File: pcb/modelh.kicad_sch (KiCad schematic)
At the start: 45 parts, among them SW1 SW_Push, U1 GD32F103C8T6, U2 AMS1117-3.3, Y1 8MHz

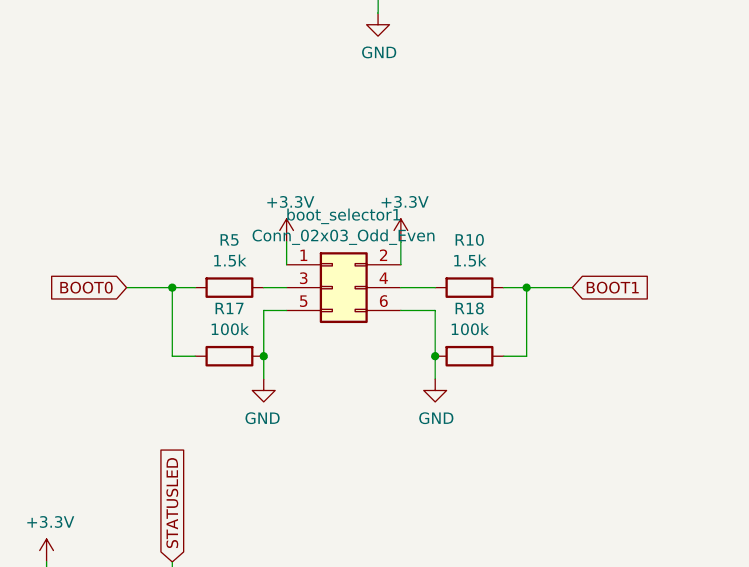
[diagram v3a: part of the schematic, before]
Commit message: Updates silkscreen to make clear boot selector
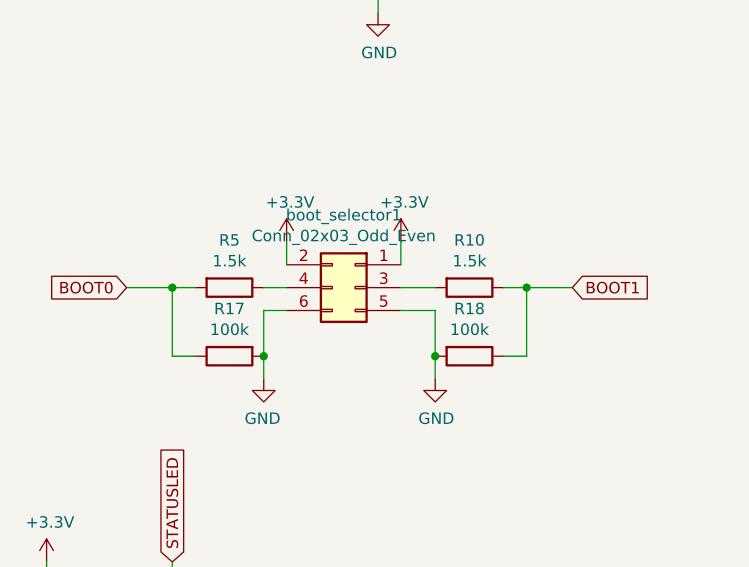
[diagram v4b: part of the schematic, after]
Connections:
- net at R10.2: now also boot_selector1.3 (Pin_3); no longer boot_selector1.4 (Pin_4)
- net at R5.1: now also boot_selector1.4 (Pin_4); no longer boot_selector1.3 (Pin_3)

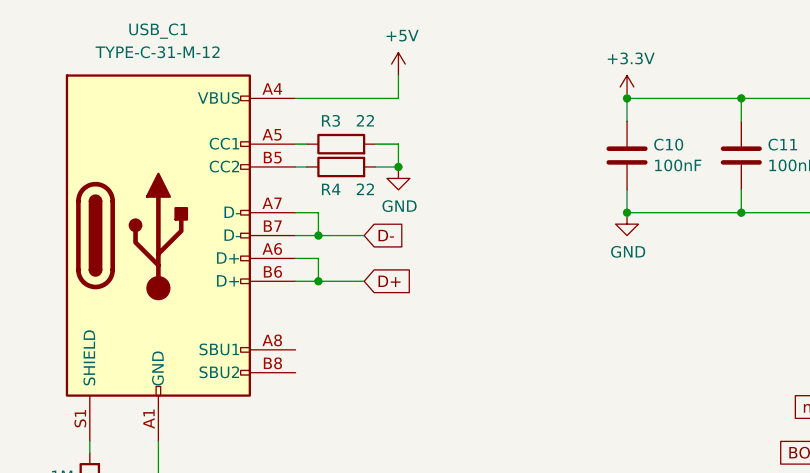
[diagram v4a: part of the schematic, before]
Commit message: Adds missing 1.5k pullup resistor to USB D+ line
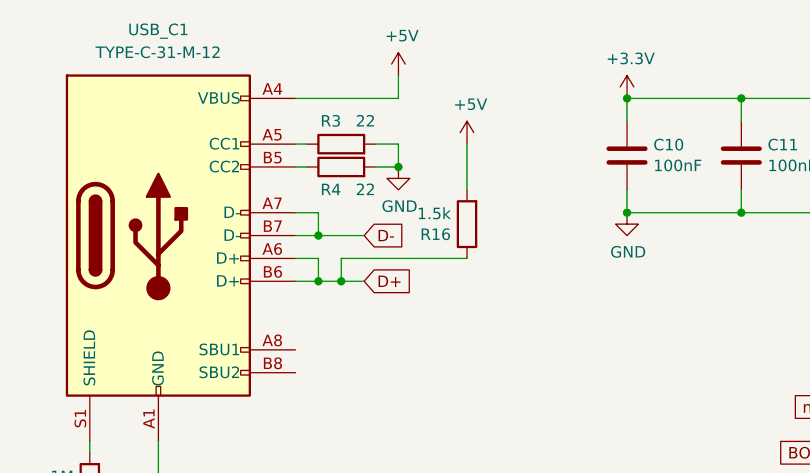
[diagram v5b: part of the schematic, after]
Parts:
- added R16: 1.5k, Resistor_SMD:R_0603_1608Metric, symbol Device:R
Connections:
- net +5V: now also R16.2
- net D+: now also R16.1
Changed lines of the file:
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@@
   (junction (at 121.92 39.37) (diameter 0) (color 0 0 0 0)
+  )
+  (junction (at 64.77 46.99) (diameter 0) (color 0 0 0 0)
   )
   (junction (at 180.34 43.18) (diameter 0) (color 0 0 0 0)
@@
     (stroke (width 0) (type default) (color 0 0 0 0))
   )
+  (wire (pts (xy 64.77 46.99) (xy 67.31 46.99))
+    (stroke (width 0) (type default) (color 0 0 0 0))
+  )
   (wire (pts (xy 67.31 88.9) (xy 72.39 88.9))
     (stroke (width 0) (type default) (color 0 0 0 0))
@@
     (stroke (width 0) (type default) (color 0 0 0 0))
   )
+  (wire (pts (xy 64.77 44.45) (xy 64.77 46.99))
+    (stroke (width 0) (type default) (color 0 0 0 0))
+  )
   (wire (pts (xy 72.39 88.9) (xy 83.82 88.9))
     (stroke (width 0) (type default) (color 0 0 0 0))
@@
     (stroke (width 0) (type default) (color 0 0 0 0))
   )
+  (wire (pts (xy 78.74 31.75) (xy 78.74 36.83))
+    (stroke (width 0) (type default) (color 0 0 0 0))
+  )
   (wire (pts (xy 248.92 49.53) (xy 255.27 49.53))
     (stroke (width 0) (type default) (color 0 0 0 0))
@@
     (stroke (width 0) (type default) (color 0 0 0 0))
   )
-  (wire (pts (xy 62.23 46.99) (xy 67.31 46.99))
+  (wire (pts (xy 62.23 46.99) (xy 64.77 46.99))
+    (stroke (width 0) (type default) (color 0 0 0 0))
+  )
+  (wire (pts (xy 78.74 44.45) (xy 64.77 44.45))
     (stroke (width 0) (type default) (color 0 0 0 0))
   )
@@
     (pin "4")
   )
+  (symbol (lib_id "power:+5V") (at 78.74 31.75 0) (unit 1)
+    (in_bom yes) (on_board yes)
+    (property "Reference" "#PWR0127" (id 0) (at 78.74 35.56 0)
+      (effects (font (size 1.27 1.27)) hide)
+    )
+    (property "Value" "+5V" (id 1) (at 79.121 27.3558 0))
+    (property "Footprint" "" (id 2) (at 78.74 31.75 0)
+      (effects (font (size 1.27 1.27)) hide)
+    )
+    (property "Datasheet" "" (id 3) (at 78.74 31.75 0)
+      (effects (font (size 1.27 1.27)) hide)
+    )
+    (pin "1")
+  )
   (symbol (lib_id "Connector:USB_C_Receptacle_USB2.0") (at 44.45 41.91 0) (unit 1)
     (in_bom yes) (on_board yes) (fields_autoplaced)
@@
     (pin "S1")
   )
+  (symbol (lib_id "Device:R") (at 78.74 40.64 180) (unit 1)
+    (in_bom yes) (on_board yes)
+    (property "Reference" "R16" (id 0) (at 76.962 41.8084 0)
+      (effects (font (size 1.27 1.27)) (justify left))
+    )
+    (property "Value" "1.5k" (id 1) (at 76.962 39.497 0)
+      (effects (font (size 1.27 1.27)) (justify left))
+    )
+    (property "Footprint" "Resistor_SMD:R_0603_1608Metric" (id 2) (at 80.518 40.64 90)
+      (effects (font (size 1.27 1.27)) hide)
+    )
+    (property "Datasheet" "~" (id 3) (at 78.74 40.64 0)
+      (effects (font (size 1.27 1.27)) hide)
+    )
+    (property "LCSC" "C22843" (id 4) (at 78.74 40.64 0)
+      (effects (font (size 1.27 1.27)) hide)
+    )
+    (pin "1")
+    (pin "2")
+  )
   (symbol (lib_id "TE-6-520315-6:6-520315-6") (at 255.27 69.85 0) (mirror x) (unit 1)
     (in_bom yes) (on_board yes)
@@
       (reference "#PWR0126") (unit 1) (value "+5V") (footprint "")
     )
+    (path "/449da5ab-c6ac-45b5-bcdc-f492eee962dc"
+      (reference "#PWR0127") (unit 1) (value "+5V") (footprint "")
+    )
     (path "/00000000-0000-0000-0000-00005f28cee3"
       (reference "C1") (unit 1) (value "10uF") (footprint "Capacitor_SMD:C_0603_1608Metric")
@@
       (reference "R15") (unit 1) (value "0") (footprint "Resistor_SMD:R_0805_2012Metric_Pad1.15x1.40mm_HandSolder")
     )
+    (path "/79b2448b-a329-4291-a39b-4d2e35c6ecb6"
+      (reference "R16") (unit 1) (value "1.5k") (footprint "Resistor_SMD:R_0603_1608Metric")
+    )
     (path "/00000000-0000-0000-0000-00005f1d1ef2"

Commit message: Update schematics and pcb
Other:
- moved on the sheet: TP1, custom_leds_A1
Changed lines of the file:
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@@
   (no_connect (at 129.54 83.82))
   (no_connect (at 129.54 81.28))
-  (wire (pts (xy 227.33 151.13) (xy 240.03 151.13))
+  (wire (pts (xy 207.01 151.13) (xy 219.71 151.13))
     (stroke (width 0) (type default) (color 0 0 0 0))
   )
@@
     (stroke (width 0) (type default) (color 0 0 0 0))
   )
-  (wire (pts (xy 227.33 153.67) (xy 240.03 153.67))
+  (wire (pts (xy 207.01 153.67) (xy 219.71 153.67))
     (stroke (width 0) (type default) (color 0 0 0 0))
   )
@@
     (stroke (width 0) (type default) (color 0 0 0 0))
   )
-  (wire (pts (xy 240.03 146.05) (xy 237.49 146.05))
+  (wire (pts (xy 219.71 146.05) (xy 217.17 146.05))
     (stroke (width 0) (type default) (color 0 0 0 0))
   )
@@
     (stroke (width 0) (type default) (color 0 0 0 0))
   )
-  (wire (pts (xy 227.33 151.13) (xy 227.33 149.86))
+  (wire (pts (xy 207.01 151.13) (xy 207.01 149.86))
     (stroke (width 0) (type default) (color 0 0 0 0))
   )
@@
     (stroke (width 0) (type default) (color 0 0 0 0))
   )
-  (wire (pts (xy 240.03 143.51) (xy 237.49 143.51))
+  (wire (pts (xy 219.71 143.51) (xy 217.17 143.51))
     (stroke (width 0) (type default) (color 0 0 0 0))
   )
@@
     (stroke (width 0) (type default) (color 0 0 0 0))
   )
-  (wire (pts (xy 237.49 148.59) (xy 240.03 148.59))
+  (wire (pts (xy 217.17 148.59) (xy 219.71 148.59))
     (stroke (width 0) (type default) (color 0 0 0 0))
   )
@@
     (stroke (width 0) (type default) (color 0 0 0 0))
   )
-  (wire (pts (xy 227.33 153.67) (xy 227.33 156.21))
+  (wire (pts (xy 207.01 153.67) (xy 207.01 156.21))
     (stroke (width 0) (type default) (color 0 0 0 0))
   )
@@
     )
   )
-  (global_label "led2" (shape input) (at 237.49 148.59 180) (fields_autoplaced)
-    (effects (font (size 1.27 1.27)) (justify right))
-    (property "Intersheet References" "${INTERSHEET_REFS}" (id 0) (at 0 0 0)
+  (global_label "led2" (shape input) (at 217.17 148.59 180) (fields_autoplaced)
+    (effects (font (size 1.27 1.27)) (justify right))
+    (property "Intersheet References" "${INTERSHEET_REFS}" (id 0) (at -20.32 0 0)
       (effects (font (size 1.27 1.27)) hide)
     )
@@
     )
   )
-  (global_label "led1" (shape input) (at 237.49 146.05 180) (fields_autoplaced)
-    (effects (font (size 1.27 1.27)) (justify right))
-    (property "Intersheet References" "${INTERSHEET_REFS}" (id 0) (at 0 0 0)
+  (global_label "led1" (shape input) (at 217.17 146.05 180) (fields_autoplaced)
+    (effects (font (size 1.27 1.27)) (justify right))
+    (property "Intersheet References" "${INTERSHEET_REFS}" (id 0) (at -20.32 0 0)
       (effects (font (size 1.27 1.27)) hide)
     )
@@
     )
   )
-  (global_label "led0" (shape input) (at 237.49 143.51 180) (fields_autoplaced)
-    (effects (font (size 1.27 1.27)) (justify right))
-    (property "Intersheet References" "${INTERSHEET_REFS}" (id 0) (at 0 0 0)
+  (global_label "led0" (shape input) (at 217.17 143.51 180) (fields_autoplaced)
+    (effects (font (size 1.27 1.27)) (justify right))
+    (property "Intersheet References" "${INTERSHEET_REFS}" (id 0) (at -20.32 0 0)
       (effects (font (size 1.27 1.27)) hide)
     )
@@
     (pin "2")
   )
-  (symbol (lib_id "power:+3.3V") (at 227.33 149.86 0) (unit 1)
-    (in_bom yes) (on_board yes)
-    (property "Reference" "#PWR0119" (id 0) (at 227.33 153.67 0)
-      (effects (font (size 1.27 1.27)) hide)
-    )
-    (property "Value" "+3.3V" (id 1) (at 227.711 145.4658 0))
-    (property "Footprint" "" (id 2) (at 227.33 149.86 0)
-      (effects (font (size 1.27 1.27)) hide)
-    )
-    (property "Datasheet" "" (id 3) (at 227.33 149.86 0)
+  (symbol (lib_id "power:+3.3V") (at 207.01 149.86 0) (unit 1)
+    (in_bom yes) (on_board yes)
+    (property "Reference" "#PWR0119" (id 0) (at 207.01 153.67 0)
+      (effects (font (size 1.27 1.27)) hide)
+    )
+    (property "Value" "+3.3V" (id 1) (at 207.391 145.4658 0))
+    (property "Footprint" "" (id 2) (at 207.01 149.86 0)
+      (effects (font (size 1.27 1.27)) hide)
+    )
+    (property "Datasheet" "" (id 3) (at 207.01 149.86 0)
       (effects (font (size 1.27 1.27)) hide)
     )
@@
     (pin "2")
   )
-  (symbol (lib_id "power:GND") (at 227.33 156.21 0) (unit 1)
-    (in_bom yes) (on_board yes)
-    (property "Reference" "#PWR0125" (id 0) (at 227.33 162.56 0)
-      (effects (font (size 1.27 1.27)) hide)
-    )
-    (property "Value" "GND" (id 1) (at 227.457 160.6042 0))
-    (property "Footprint" "" (id 2) (at 227.33 156.21 0)
-      (effects (font (size 1.27 1.27)) hide)
-    )
-    (property "Datasheet" "" (id 3) (at 227.33 156.21 0)
+  (symbol (lib_id "power:GND") (at 207.01 156.21 0) (unit 1)
+    (in_bom yes) (on_board yes)
+    (property "Reference" "#PWR0125" (id 0) (at 207.01 162.56 0)
+      (effects (font (size 1.27 1.27)) hide)
+    )
+    (property "Value" "GND" (id 1) (at 207.137 160.6042 0))
+    (property "Footprint" "" (id 2) (at 207.01 156.21 0)
+      (effects (font (size 1.27 1.27)) hide)
+    )
+    (property "Datasheet" "" (id 3) (at 207.01 156.21 0)
       (effects (font (size 1.27 1.27)) hide)
     )
@@
     (pin "5")
   )
-  (symbol (lib_id "Connector:TestPoint") (at 213.36 147.32 180) (unit 1)
-    (in_bom yes) (on_board yes)
-    (property "Reference" "TP1" (id 0) (at 214.8332 147.9804 0)
+  (symbol (lib_id "Connector:TestPoint") (at 193.04 147.32 180) (unit 1)
+    (in_bom yes) (on_board yes)
+    (property "Reference" "TP1" (id 0) (at 194.5132 147.9804 0)
       (effects (font (size 1.27 1.27)) (justify right))
     )
-    (property "Value" "TestPoint" (id 1) (at 214.8332 150.2918 0)
+    (property "Value" "TestPoint" (id 1) (at 194.5132 150.2918 0)
       (effects (font (size 1.27 1.27)) (justify right))
     )
-    (property "Footprint" "TestPoint:TestPoint_THTPad_D1.5mm_Drill0.7mm" (id 2) (at 208.28 147.32 0)
-      (effects (font (size 1.27 1.27)) hide)
-    )
-    (property "Datasheet" "~" (id 3) (at 208.28 147.32 0)
+    (property "Footprint" "TestPoint:TestPoint_THTPad_D1.5mm_Drill0.7mm" (id 2) (at 187.96 147.32 0)
+      (effects (font (size 1.27 1.27)) hide)
+    )
+    (property "Datasheet" "~" (id 3) (at 187.96 147.32 0)
       (effects (font (size 1.27 1.27)) hide)
     )
@@
     (pin "3")
   )
-  (symbol (lib_id "power:+5V") (at 213.36 147.32 0) (unit 1)
-    (in_bom yes) (on_board yes)
-    (property "Reference" "#PWR0126" (id 0) (at 213.36 151.13 0)
-      (effects (font (size 1.27 1.27)) hide)
-    )
-    (property "Value" "+5V" (id 1) (at 213.741 142.9258 0))
-    (property "Footprint" "" (id 2) (at 213.36 147.32 0)
-      (effects (font (size 1.27 1.27)) hide)
-    )
-    (property "Datasheet" "" (id 3) (at 213.36 147.32 0)
+  (symbol (lib_id "power:+5V") (at 193.04 147.32 0) (unit 1)
+    (in_bom yes) (on_board yes)
+    (property "Reference" "#PWR0126" (id 0) (at 193.04 151.13 0)
+      (effects (font (size 1.27 1.27)) hide)
+    )
+    (property "Value" "+5V" (id 1) (at 193.421 142.9258 0))
+    (property "Footprint" "" (id 2) (at 193.04 147.32 0)
+      (effects (font (size 1.27 1.27)) hide)
+    )
+    (property "Datasheet" "" (id 3) (at 193.04 147.32 0)
       (effects (font (size 1.27 1.27)) hide)
     )
@@
     (pin "2")
   )
-  (symbol (lib_id "Connector_Generic:Conn_01x05") (at 245.11 148.59 0) (unit 1)
-    (in_bom yes) (on_board yes)
-    (property "Reference" "custom_leds_A1" (id 0) (at 247.142 147.5232 0)
-      (effects (font (size 1.27 1.27)) (justify left))
-    )
-    (property "Value" "Conn_01x05" (id 1) (at 247.142 149.8346 0)
-      (effects (font (size 1.27 1.27)) (justify left))
-    )
-    (property "Footprint" "Connector_PinSocket_2.54mm:PinSocket_1x05_P2.54mm_Vertical" (id 2) (at 245.11 148.59 0)
-      (effects (font (size 1.27 1.27)) hide)
-    )
-    (property "Datasheet" "~" (id 3) (at 245.11 148.59 0)
-      (effects (font (size 1.27 1.27)) hide)
-    )
+  (symbol (lib_id "Connector_Generic:Conn_01x05") (at 224.79 148.59 0) (unit 1)
+    (in_bom yes) (on_board yes)
+    (property "Reference" "custom_leds_A1" (id 0) (at 226.822 147.5232 0)
+      (effects (font (size 1.27 1.27)) (justify left))
+    )
+    (property "Value" "Conn_01x05" (id 1) (at 226.822 149.8346 0)
+      (effects (font (size 1.27 1.27)) (justify left))
+    )
+    (property "Footprint" "Connector_PinSocket_2.54mm:PinSocket_1x05_P2.54mm_Vertical" (id 2) (at 224.79 148.59 0)
+      (effects (font (size 1.27 1.27)) hide)
+    )
+    (property "Datasheet" "~" (id 3) (at 224.79 148.59 0)
+      (effects (font (size 1.27 1.27)) hide)
+    )
